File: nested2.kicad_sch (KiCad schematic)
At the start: 1 part, among them U3 TPS22950YBHR

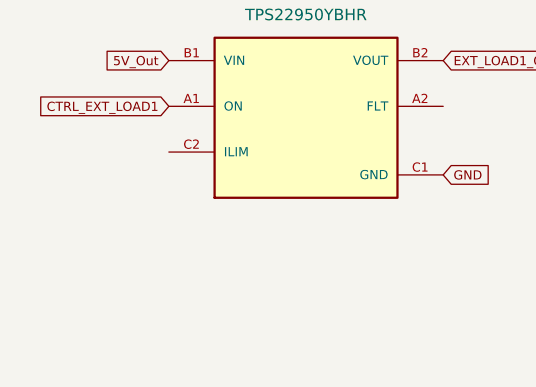
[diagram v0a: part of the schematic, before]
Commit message: Removed old backups and updated KiCad files
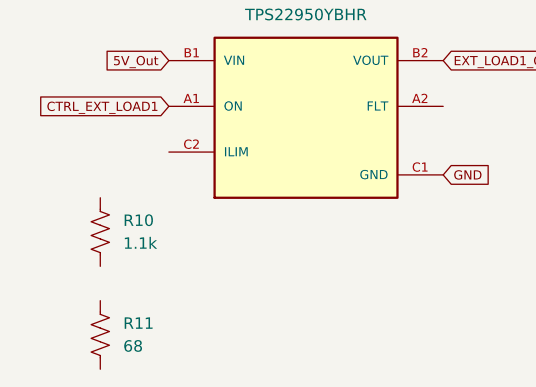
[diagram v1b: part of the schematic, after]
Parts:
- added R10: 1.1k, 1206W4F1101T5E:RESC3115X65N, symbol Device:R_US
- added R11: 68, 1206W4F6800T5E:RESC3115X65N, symbol Device:R_US
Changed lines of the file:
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@@
+	)
+	(symbol
+		(lib_id "Device:R_US")
+		(at 66.04 115.57 0)
+		(unit 1)
+		(exclude_from_sim no)
+		(in_bom yes)
+		(on_board yes)
+		(dnp no)
+		(fields_autoplaced yes)
+		(property "Reference" "R10"
+			(at 68.58 114.2999 0)
+			(effects
+				(font
+					(size 1.27 1.27)
+				)
+				(justify left)
+			)
+		)
+		(property "Value" "1.1k"
+			(at 68.58 116.8399 0)
+			(effects
+				(font
+					(size 1.27 1.27)
+				)
+				(justify left)
+			)
+		)
+		(property "Footprint" "1206W4F1101T5E:RESC3115X65N"
+			(at 67.056 115.824 90)
+			(effects
+				(font
+					(size 1.27 1.27)
+				)
+				(hide yes)
+			)
+		)
+		(property "Datasheet" "~"
+			(at 66.04 115.57 0)
+			(effects
+				(font
+					(size 1.27 1.27)
+				)
+				(hide yes)
+			)
+		)
+		(property "Description" "Resistor, US symbol"
+			(at 66.04 115.57 0)
+			(effects
+				(font
+					(size 1.27 1.27)
+				)
+				(hide yes)
+			)
+		)
+		(pin "1"
+		)
+		(pin "2"
+		)
+		(instances
+			(project ""
+				(path "/d1463c6f-2f5e-4460-8cd2-c7ccf4d8def7/5921a43a-66b4-4a5d-9407-3d9130778733"
+					(reference "R10")
+					(unit 1)
+				)
+			)
+		)
+	)
+	(symbol
+		(lib_id "Device:R_US")
+		(at 66.04 127 0)
+		(unit 1)
+		(exclude_from_sim no)
+		(in_bom yes)
+		(on_board yes)
+		(dnp no)
+		(fields_autoplaced yes)
+		(property "Reference" "R11"
+			(at 68.58 125.7299 0)
+			(effects
+				(font
+					(size 1.27 1.27)
+				)
+				(justify left)
+			)
+		)
+		(property "Value" "68"
+			(at 68.58 128.2699 0)
+			(effects
+				(font
+					(size 1.27 1.27)
+				)
+				(justify left)
+			)
+		)
+		(property "Footprint" "1206W4F6800T5E:RESC3115X65N"
+			(at 67.056 127.254 90)
+			(effects
+				(font
+					(size 1.27 1.27)
+				)
+				(hide yes)
+			)
+		)
+		(property "Datasheet" "~"
+			(at 66.04 127 0)
+			(effects
+				(font
+					(size 1.27 1.27)
+				)
+				(hide yes)
+			)
+		)
+		(property "Description" "Resistor, US symbol"
+			(at 66.04 127 0)
+			(effects
+				(font
+					(size 1.27 1.27)
+				)
+				(hide yes)
+			)
+		)
+		(pin "1"
+		)
+		(pin "2"
+		)
+		(instances
+			(project "EEE3088F Design project"
+				(path "/d1463c6f-2f5e-4460-8cd2-c7ccf4d8def7/5921a43a-66b4-4a5d-9407-3d9130778733"
+					(reference "R11")
+					(unit 1)
+				)
+			)
+		)
 	)
 	(symbol

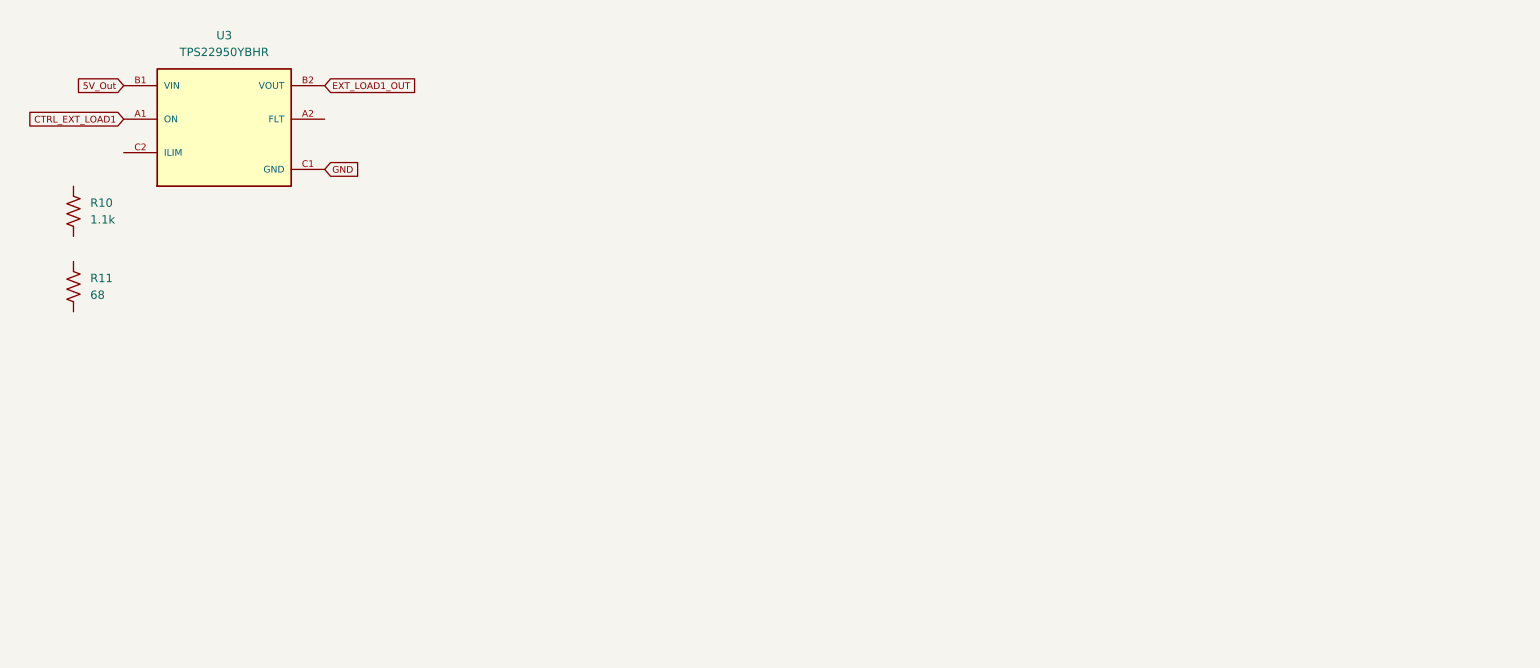
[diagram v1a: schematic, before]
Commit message: Removed old backups and updated KiCad files
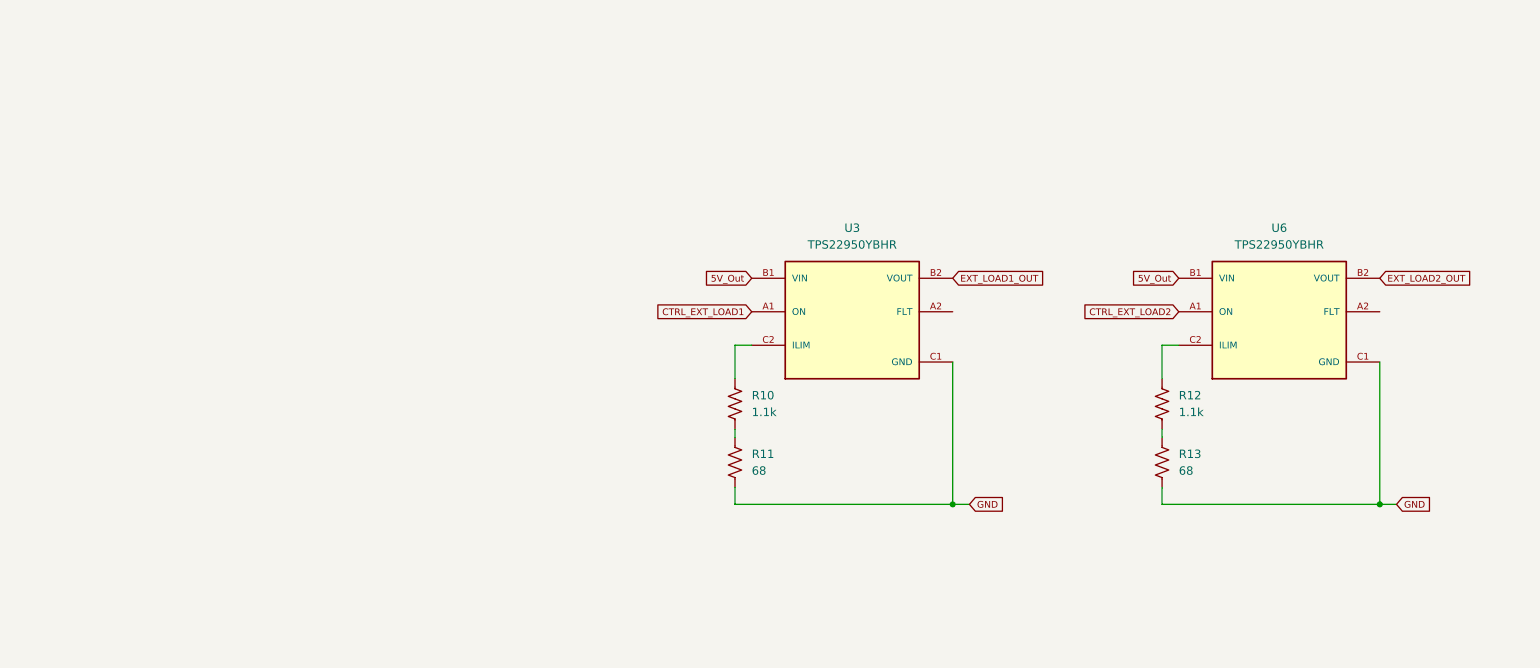
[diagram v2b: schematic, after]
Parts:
- added R12: 1.1k, Resistor_SMD:R_1206_3216Metric_Pad1.30x1.75mm_HandSolder, symbol Device:R_US
- added R13: 68, Resistor_SMD:R_1206_3216Metric_Pad1.30x1.75mm_HandSolder, symbol Device:R_US
- added U6: TPS22950YBHR, TPS22950YBHR:IC_TPS22950YBHR, symbol TPS22950YBHR:TPS22950YBHR
- R10: footprint 1206W4F1101T5E:RESC3115X65N -> Resistor_SMD:R_1206_3216Metric_Pad1.30x1.75mm_HandSolder
- R11: footprint 1206W4F6800T5E:RESC3115X65N -> Resistor_SMD:R_1206_3216Metric_Pad1.30x1.75mm_HandSolder
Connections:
- net 5V_Out: now also U6.B1 (VIN)
- net GND: now also R11.2, R13.2, U6.C1 (GND)
- net at R10.1: now also U3.C2 (ILIM)
- net at R10.2: now also R11.1
- new net: R12.2, R13.1
- new net: R12.1, U6.C2 (ILIM)
- new net CTRL_EXT_LOAD2: U6.A1 (ON)
- new net EXT_LOAD2_OUT: U6.B2 (VOUT)
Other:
- moved on the sheet: R10, R11, U3

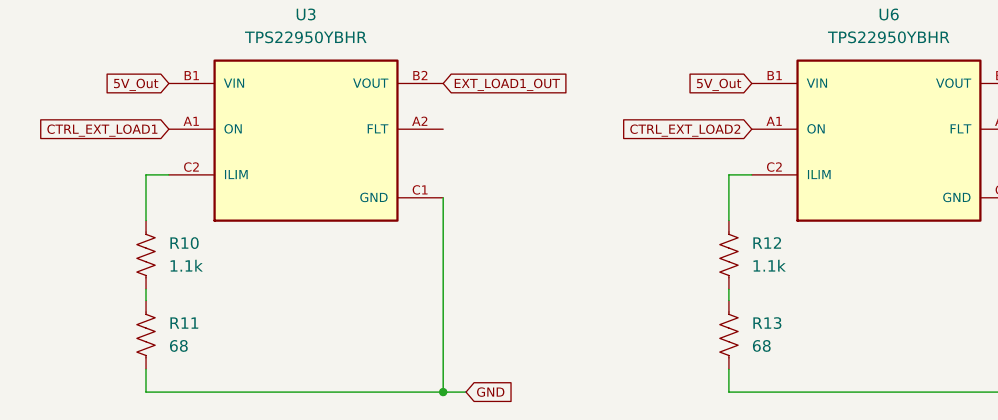
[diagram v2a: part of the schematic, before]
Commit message: Removed old backups and updated KiCad files
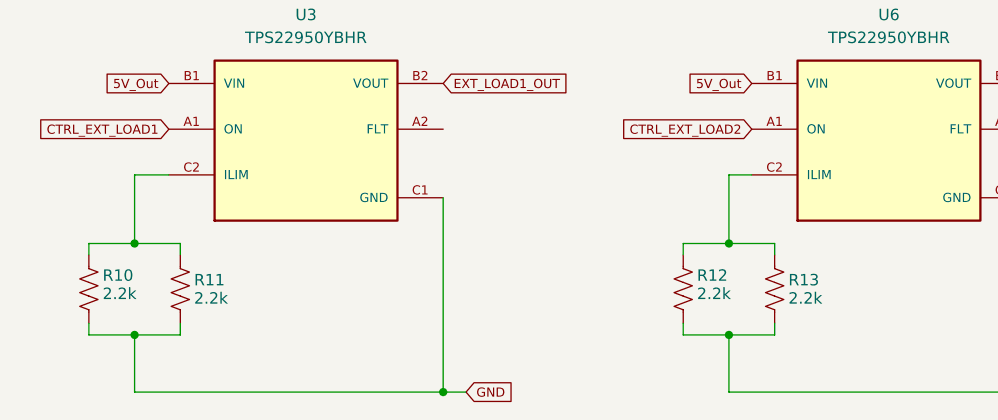
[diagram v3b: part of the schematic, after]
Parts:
- R10, R12: value 1.1k -> 2.2k; footprint Resistor_SMD:R_1206_3216Metric_Pad1.30x1.75mm_HandSolder -> Resistor_SMD:R_0603_1608Metric_Pad0.98x0.95mm_HandSolder; LCSC (none) -> C4190
- R11, R13: value 68 -> 2.2k; footprint Resistor_SMD:R_1206_3216Metric_Pad1.30x1.75mm_HandSolder -> Resistor_SMD:R_0603_1608Metric_Pad0.98x0.95mm_HandSolder; LCSC (none) -> C4190
- U3, U6: LCSC (none) -> C3230039
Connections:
- net GND: now also R10.2, R12.2
- net at R10.1, U3.C2 (ILIM): now also R11.1
- net at R13.1: now also R12.1, U6.C2 (ILIM); no longer R12.2
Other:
- moved on the sheet: R10

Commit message: Removed old backups and update KiCad files
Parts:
- added TP11, TP12: TestPoint, TestPoint:TestPoint_Pad_1.0x1.0mm, symbol Connector:TestPoint
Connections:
- net EXT_LOAD1_OUT: now also TP11.1
- net EXT_LOAD2_OUT: now also TP12.1
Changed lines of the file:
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@@
+	)
+	(junction
+		(at 266.7 125.73)
+		(diameter 0)
+		(color 0 0 0 0)
 	)
 	(junction
@@
 		(color 0 0 0 0)
 	)
+	(junction
+		(at 201.93 125.73)
+		(diameter 0)
+		(color 0 0 0 0)
+	)
 	(wire
 		(pts
@@
 	(wire
 		(pts
+			(xy 201.93 125.73) (xy 199.39 125.73)
+		)
+		(stroke
+			(width 0)
+			(type default)
+		)
+	)
+	(wire
+		(pts
 			(xy 231.14 153.67) (xy 236.22 153.67)
 		)
@@
 	(wire
 		(pts
+			(xy 266.7 125.73) (xy 264.16 125.73)
+		)
+		(stroke
+			(width 0)
+			(type default)
+		)
+	)
+	(wire
+		(pts
 			(xy 264.16 160.02) (xy 264.16 138.43)
 		)
@@
 	(wire
 		(pts
+			(xy 205.74 125.73) (xy 201.93 125.73)
+		)
+		(stroke
+			(width 0)
+			(type default)
+		)
+	)
+	(wire
+		(pts
 			(xy 165.1 143.51) (xy 170.18 143.51)
 		)
@@
 		(pts
 			(xy 160.02 153.67) (xy 165.1 153.67)
+		)
+		(stroke
+			(width 0)
+			(type default)
+		)
+	)
+	(wire
+		(pts
+			(xy 270.51 125.73) (xy 266.7 125.73)
 		)
 		(stroke
@@
 	(global_label "EXT_LOAD1_OUT"
 		(shape input)
-		(at 199.39 125.73 0)
+		(at 205.74 125.73 0)
 		(fields_autoplaced yes)
 		(effects
@@
 		)
 		(property "Intersheetrefs" "${INTERSHEET_REFS}"
-			(at 185.1487 125.73 0)
+			(at 191.4987 125.73 0)
 			(effects
 				(font
@@
 	(global_label "EXT_LOAD2_OUT"
 		(shape input)
-		(at 264.16 125.73 0)
+		(at 270.51 125.73 0)
 		(fields_autoplaced yes)
 		(effects
@@
 		)
 		(property "Intersheetrefs" "${INTERSHEET_REFS}"
-			(at 249.9187 125.73 0)
+			(at 256.2687 125.73 0)
 			(effects
 				(font
@@
 	)
 	(symbol
+		(lib_id "Connector:TestPoint")
+		(at 266.7 125.73 0)
+		(unit 1)
+		(exclude_from_sim no)
+		(in_bom yes)
+		(on_board yes)
+		(dnp no)
+		(fields_autoplaced yes)
+		(property "Reference" "TP12"
+			(at 269.24 121.1579 0)
+			(effects
+				(font
+					(size 1.27 1.27)
+				)
+				(justify left)
+			)
+		)
+		(property "Value" "TestPoint"
+			(at 269.24 123.6979 0)
+			(effects
+				(font
+					(size 1.27 1.27)
+				)
+				(justify left)
+			)
+		)
+		(property "Footprint" "TestPoint:TestPoint_Pad_1.0x1.0mm"
+			(at 271.78 125.73 0)
+			(effects
+				(font
+					(size 1.27 1.27)
+				)
+				(hide yes)
+			)
+		)
+		(property "Datasheet" "~"
+			(at 271.78 125.73 0)
+			(effects
+				(font
+					(size 1.27 1.27)
+				)
+				(hide yes)
+			)
+		)
+		(property "Description" "test point"
+			(at 266.7 125.73 0)
+			(effects
+				(font
+					(size 1.27 1.27)
+				)
+				(hide yes)
+			)
+		)
+		(pin "1"
+		)
+		(instances
+			(project "EEE3088F Design project"
+				(path "/d1463c6f-2f5e-4460-8cd2-c7ccf4d8def7/5921a43a-66b4-4a5d-9407-3d9130778733"
+					(reference "TP12")
+					(unit 1)
+				)
+			)
+		)
+	)
+	(symbol
 		(lib_id "Device:R_US")
 		(at 236.22 148.59 0)
@@
 					(unit 1)
 				)
+			)
+		)
+	)
+	(symbol
+		(lib_id "Connector:TestPoint")
+		(at 201.93 125.73 0)
+		(unit 1)
+		(exclude_from_sim no)
+		(in_bom yes)
+		(on_board yes)
+		(dnp no)
+		(fields_autoplaced yes)
+		(property "Reference" "TP11"
+			(at 204.47 121.1579 0)
+			(effects
+				(font
+					(size 1.27 1.27)
+				)
+				(justify left)
+			)
+		)
+		(property "Value" "TestPoint"
+			(at 204.47 123.6979 0)
+			(effects
+				(font
+					(size 1.27 1.27)
+				)
+				(justify left)
+			)
+		)
+		(property "Footprint" "TestPoint:TestPoint_Pad_1.0x1.0mm"
+			(at 207.01 125.73 0)
+			(effects
+				(font
+					(size 1.27 1.27)
+				)
+				(hide yes)
+			)
+		)
+		(property "Datasheet" "~"
+			(at 207.01 125.73 0)
+			(effects
+				(font
+					(size 1.27 1.27)
+				)
+				(hide yes)
+			)
+		)
+		(property "Description" "test point"
+			(at 201.93 125.73 0)
+			(effects
+				(font
+					(size 1.27 1.27)
+				)
+				(hide yes)
+			)
+		)
+		(pin "1"
+		)
+		(instances
+			(project ""
+				(path "/d1463c6f-2f5e-4460-8cd2-c7ccf4d8def7/5921a43a-66b4-4a5d-9407-3d9130778733"
+					(reference "TP11")
+					(unit 1)
+				)

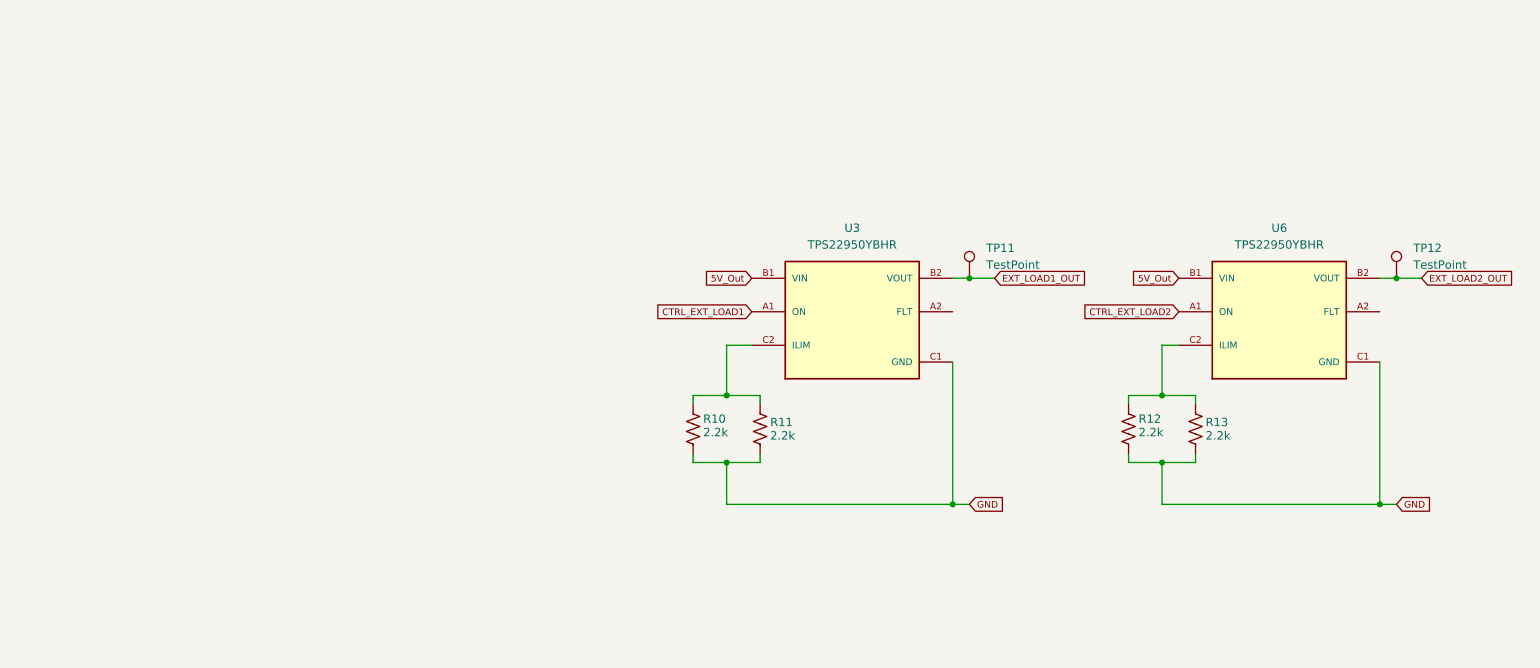
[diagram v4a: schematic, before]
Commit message: Removed old backups and updated KiCad files
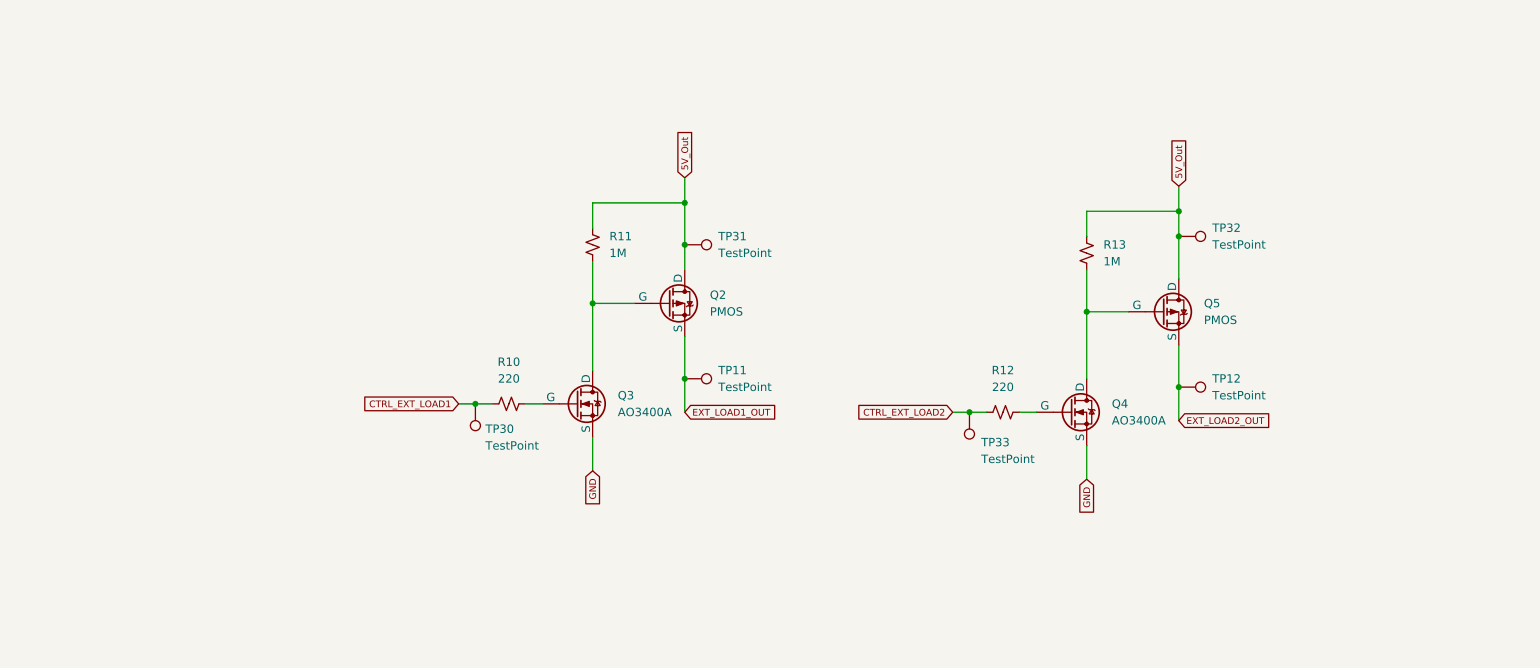
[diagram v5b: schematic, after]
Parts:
- removed R10, R11, R12, R13: 2.2k, Resistor_SMD:R_0603_1608Metric_Pad0.98x0.95mm_HandSolder, symbol Device:R_US
- removed U3, U6: TPS22950YBHR, TPS22950YBHR:IC_TPS22950YBHR, symbol TPS22950YBHR:TPS22950YBHR
- added Q2, Q5: PMOS, Package_TO_SOT_SMD:SOT-23_Handsoldering, symbol Simulation_SPICE:PMOS
- added Q3, Q4: AO3400A, Package_TO_SOT_SMD:SOT-23-3, symbol Simulation_SPICE:NMOS
- added R10, R12: 220, Resistor_SMD:R_0603_1608Metric_Pad0.98x0.95mm_HandSolder, symbol Device:R_Small_US
- added R11, R13: 1M, Resistor_SMD:R_1206_3216Metric_Pad1.30x1.75mm_HandSolder, symbol Device:R_Small_US
- added TP30, TP31, TP32, TP33: TestPoint, TestPoint:TestPoint_Pad_1.0x1.0mm, symbol Connector:TestPoint
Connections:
- net 5V_Out: now also Q2.1 (D), Q5.1 (D), R11.2, R13.2, TP31.1, TP32.1
- net CTRL_EXT_LOAD1: now also R10.1, TP30.1
- net CTRL_EXT_LOAD2: now also R12.1, TP33.1
- net EXT_LOAD1_OUT: now also Q2.3 (S)
- net EXT_LOAD2_OUT: now also Q5.3 (S)
- net GND: now also Q3.3 (S), Q4.3 (S)
- new net: Q4.2 (G), R12.2
- new net: Q2.2 (G), Q3.1 (D), R11.1
- new net: Q3.2 (G), R10.2
- new net: Q4.1 (D), Q5.2 (G), R13.1
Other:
- moved on the sheet: TP11, TP12
